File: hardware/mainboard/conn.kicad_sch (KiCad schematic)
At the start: 33 parts, among them J1 Conn_01x40_Shielded, J2 Conn_01x40_Shielded, J3 EAR, J4 Conn_02x06_Top_Bottom, P1 M2_SOCKET_E, SW1 SW_Push, SW2 SW_Push, SW3 SW_Push, U1 LIFCL_40_CABGA400, U10 Si52112-B, U9 74AHC1G126, Y1 25MHz

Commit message: Working on layout
Signed-off-by: David Shah <dave@ds0.me>
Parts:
- removed R27: 10k, Resistor_SMD:R_0402_1005Metric, symbol Device:R_Small
- removed SW2: SW_Push, Button_Switch_THT:SW_Tactile_SPST_Angled_PTS645Vx31-2LFS, symbol Switch:SW_Push
- J3: footprint Connector_PinHeader_2.54mm:PinHeader_2x03_P2.54mm_Horizontal -> Connector_PinHeader_2.00mm:PinHeader_2x03_P2.00mm_Horizontal
- renumbered SW3 to SW2
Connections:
- net BTN2 is gone; now on net BTN1: R28.1, SW2.2
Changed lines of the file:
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@@
   (junction (at 184.15 62.23) (diameter 1.016) (color 0 0 0 0))
   (junction (at 213.36 209.55) (diameter 1.016) (color 0 0 0 0))
-  (junction (at 213.36 218.44) (diameter 1.016) (color 0 0 0 0))
   (junction (at 232.41 209.55) (diameter 1.016) (color 0 0 0 0))
-  (junction (at 232.41 218.44) (diameter 1.016) (color 0 0 0 0))
   (junction (at 232.41 227.33) (diameter 1.016) (color 0 0 0 0))
   (junction (at 260.35 218.44) (diameter 1.016) (color 0 0 0 0))
@@
     (stroke (width 0) (type solid) (color 0 0 0 0))
   )
+  (wire (pts (xy 213.36 209.55) (xy 213.36 227.33))
+    (stroke (width 0) (type solid) (color 0 0 0 0))
+  )
   (wire (pts (xy 213.36 209.55) (xy 218.44 209.55))
     (stroke (width 0) (type solid) (color 0 0 0 0))
   )
-  (wire (pts (xy 213.36 218.44) (xy 213.36 209.55))
-    (stroke (width 0) (type solid) (color 0 0 0 0))
-  )
-  (wire (pts (xy 213.36 218.44) (xy 218.44 218.44))
-    (stroke (width 0) (type solid) (color 0 0 0 0))
-  )
-  (wire (pts (xy 213.36 227.33) (xy 213.36 218.44))
-    (stroke (width 0) (type solid) (color 0 0 0 0))
-  )
   (wire (pts (xy 215.9 143.51) (xy 209.55 143.51))
     (stroke (width 0) (type solid) (color 0 0 0 0))
@@
     (stroke (width 0) (type solid) (color 0 0 0 0))
   )
-  (wire (pts (xy 228.6 218.44) (xy 232.41 218.44))
-    (stroke (width 0) (type solid) (color 0 0 0 0))
-  )
   (wire (pts (xy 228.6 227.33) (xy 232.41 227.33))
     (stroke (width 0) (type solid) (color 0 0 0 0))
@@
     (stroke (width 0) (type solid) (color 0 0 0 0))
   )
-  (wire (pts (xy 232.41 215.9) (xy 232.41 218.44))
-    (stroke (width 0) (type solid) (color 0 0 0 0))
-  )
-  (wire (pts (xy 232.41 218.44) (xy 247.65 218.44))
-    (stroke (width 0) (type solid) (color 0 0 0 0))
-  )
   (wire (pts (xy 232.41 224.79) (xy 232.41 227.33))
     (stroke (width 0) (type solid) (color 0 0 0 0))
@@
     (stroke (width 0) (type solid) (color 0 0 0 0))
   )
-  (wire (pts (xy 234.95 215.9) (xy 232.41 215.9))
-    (stroke (width 0) (type solid) (color 0 0 0 0))
-  )
   (wire (pts (xy 234.95 224.79) (xy 232.41 224.79))
-    (stroke (width 0) (type solid) (color 0 0 0 0))
-  )
-  (wire (pts (xy 252.73 218.44) (xy 260.35 218.44))
     (stroke (width 0) (type solid) (color 0 0 0 0))
   )
@@
     )
   )
-  (global_label "BTN1" (shape output) (at 234.95 215.9 0)
-    (effects (font (size 1.27 1.27)) (justify left))
-    (property "Intersheet References" "${INTERSHEET_REFS}" (id 0) (at 243.6647 215.8206 0)
-      (effects (font (size 1.27 1.27)) (justify left) hide)
-    )
-  )
-  (global_label "BTN2" (shape output) (at 234.95 224.79 0)
+  (global_label "BTN1" (shape output) (at 234.95 224.79 0)
     (effects (font (size 1.27 1.27)) (justify left))
     (property "Intersheet References" "${INTERSHEET_REFS}" (id 0) (at 243.6647 224.7106 0)
@@
     (pin "2")
   )
-  (symbol (lib_id "Device:R_Small") (at 250.19 218.44 90) (unit 1)
-    (in_bom yes) (on_board yes)
-    (property "Reference" "R27" (id 0) (at 250.19 213.4932 90))
-    (property "Value" "10k" (id 1) (at 250.19 215.792 90))
-    (property "Footprint" "Resistor_SMD:R_0402_1005Metric" (id 2) (at 250.19 218.44 0)
-      (effects (font (size 1.27 1.27)) hide)
-    )
-    (property "Datasheet" "~" (id 3) (at 250.19 218.44 0)
-      (effects (font (size 1.27 1.27)) hide)
-    )
-    (pin "1")
-    (pin "2")
-  )
   (symbol (lib_id "Device:R_Small") (at 250.19 227.33 90) (unit 1)
     (in_bom yes) (on_board yes)
@@
     (pin "2")
   )
-  (symbol (lib_id "Switch:SW_Push") (at 223.52 218.44 0) (unit 1)
-    (in_bom yes) (on_board yes)
-    (property "Reference" "SW2" (id 0) (at 223.52 211.3088 0))
-    (property "Value" "SW_Push" (id 1) (at 223.52 213.6075 0))
-    (property "Footprint" "Button_Switch_THT:SW_Tactile_SPST_Angled_PTS645Vx31-2LFS" (id 2) (at 223.52 213.36 0)
-      (effects (font (size 1.27 1.27)) hide)
-    )
-    (property "Datasheet" "~" (id 3) (at 223.52 213.36 0)
-      (effects (font (size 1.27 1.27)) hide)
-    )
-    (pin "1")
-    (pin "2")
-  )
   (symbol (lib_id "Switch:SW_Push") (at 223.52 227.33 0) (unit 1)
     (in_bom yes) (on_board yes)
-    (property "Reference" "SW3" (id 0) (at 223.52 220.1988 0))
+    (property "Reference" "SW2" (id 0) (at 223.52 220.199 0))
     (property "Value" "SW_Push" (id 1) (at 223.52 222.4975 0))
     (property "Footprint" "Button_Switch_THT:SW_Tactile_SPST_Angled_PTS645Vx31-2LFS" (id 2) (at 223.52 222.25 0)
@@
       (effects (font (size 1.27 1.27)) (justify left))
     )
-    (property "Footprint" "Connector_PinHeader_2.54mm:PinHeader_2x03_P2.54mm_Horizontal" (id 2) (at 220.98 148.59 0)
-      (effects (font (size 1.27 1.27)) hide)
-    )
+    (property "Footprint" "Connector_PinHeader_2.00mm:PinHeader_2x03_P2.00mm_Horizontal" (id 2) (at 220.98 148.59 0)
+      (effects (font (size 1.27 1.27)) hide)
+    )

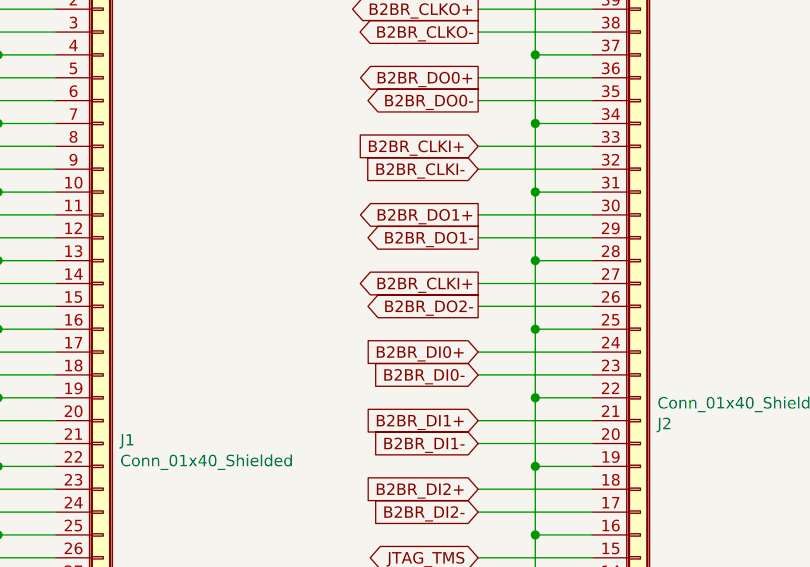
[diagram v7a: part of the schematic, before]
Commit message: Interboard pair routing
Signed-off-by: David Shah <dave@ds0.me>
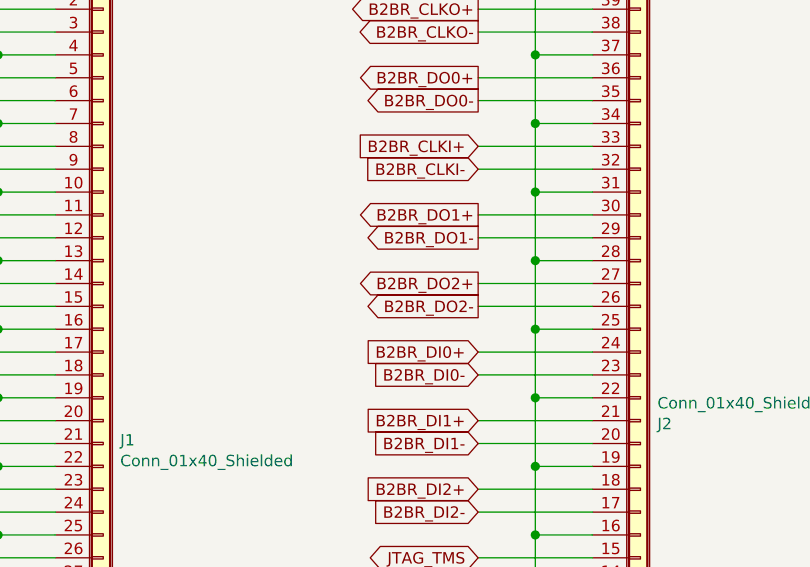
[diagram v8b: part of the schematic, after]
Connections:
- net B2BR_CLKI+: no longer J2.27 (Pin_27)
- new net B2BR_DO2+: J2.27 (Pin_27)
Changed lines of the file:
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@@
     )
   )
-  (global_label "B2BR_CLKI+" (shape output) (at 129.54 160.02 180)
+  (global_label "B2BR_DO2+" (shape output) (at 129.54 160.02 180)
     (effects (font (size 1.27 1.27)) (justify right))
-    (property "Intersheet References" "${INTERSHEET_REFS}" (id 0) (at 113.8705 159.9406 0)
+    (property "Intersheet References" "${INTERSHEET_REFS}" (id 0) (at 114.2334 159.9406 0)
       (effects (font (size 1.27 1.27)) (justify right) hide)
     )
